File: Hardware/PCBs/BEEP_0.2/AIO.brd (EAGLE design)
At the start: 106.2 x 69.1 mm, 85 parts, among them IC1 ULN2803ASOP18, IC2 ULN2803ASOP18, IC3 74HC238SSOP, IC4 74HC238SSOP, IC5 TS34119SMD, U2 TB6612FNG, U3 ATXMEGA64D3-AU, X1 MICROMATCH-4, X10 MICROMATCH-10, X3 MICROMATCH-8, X4 MICROMATCH-8, X5 MICROMATCH-8, X8 MICROMATCH-8, X9 MICROMATCH-4

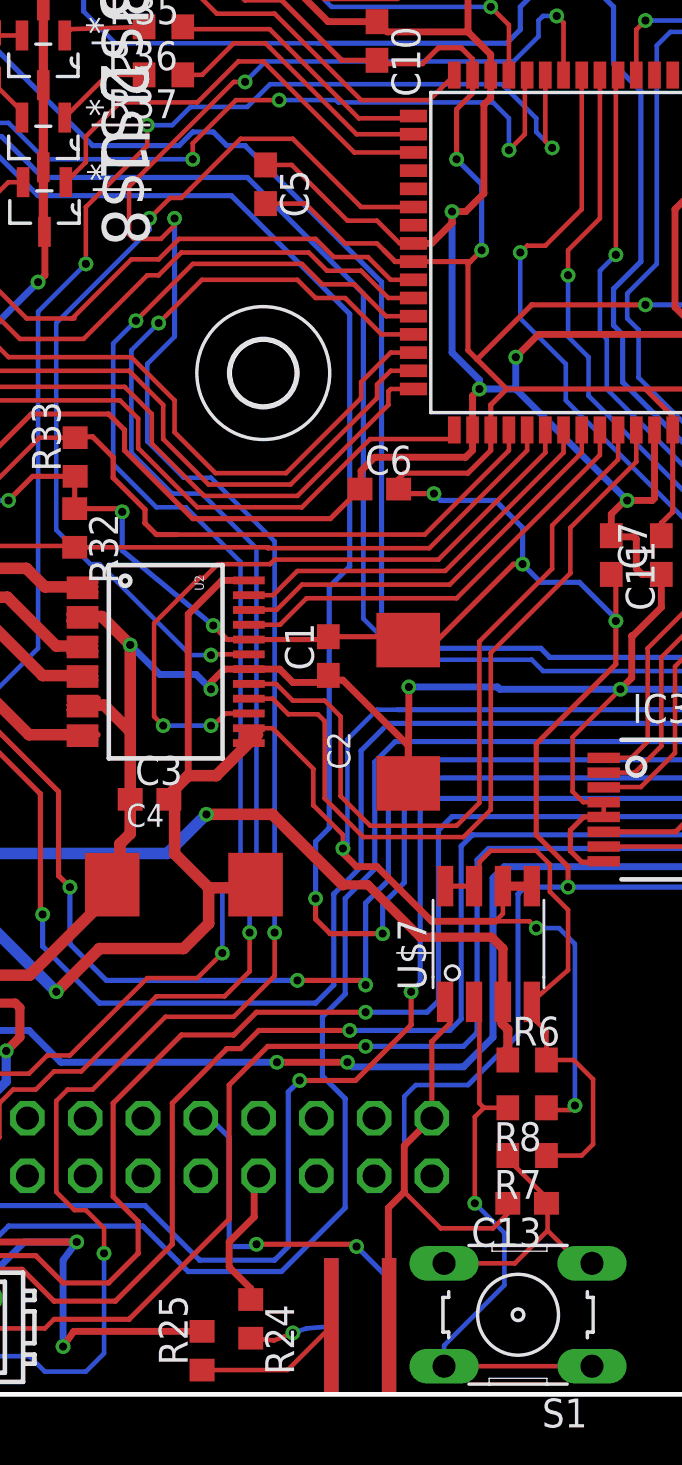
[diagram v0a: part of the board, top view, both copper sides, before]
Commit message: add poweroff line to atxmega
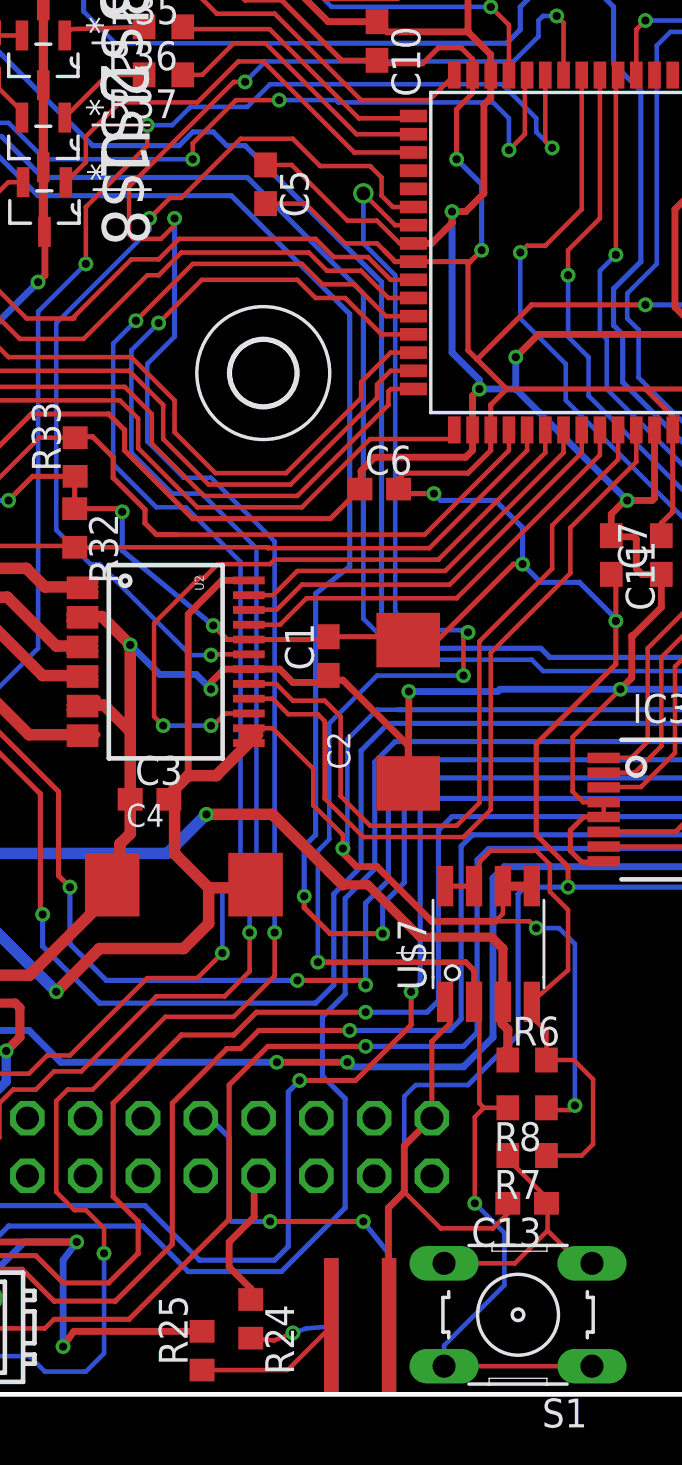
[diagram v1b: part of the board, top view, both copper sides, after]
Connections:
- removed net N$18: R8.2, S1.1, S1.2, U$7.2
- new net POWER_OFF: R8.2, S1.1, S1.2, U$7.2, U3.23
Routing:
- net POWER_OFF: track 0.00 -> 78.8 mm, vias 0 -> 5
- net N$18: track 25.7 -> 0.00 mm, vias 1 -> 0
- net +3V3: track 371.9 -> 368.6 mm
- net IR_LED_K6_OUT: track 114.9 -> 115.4 mm
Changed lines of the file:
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@@
 <wire x1="67.515" y1="36.3" x2="70.1" y2="36.3" width="0.3048" layer="1"/>
 <via x="51.9" y="36.7" extent="1-16" drill="0.3556" shape="octagon"/>
-<wire x1="42.2" y1="36.8" x2="38.3" y2="36.8" width="0.3048" layer="16"/>
-<via x="38.3" y="36.8" extent="1-16" drill="0.3556" shape="octagon"/>
-<wire x1="38.3" y1="36.8" x2="38.3" y2="35.79" width="0.3048" layer="1"/>
+<wire x1="42.2" y1="36.6" x2="38.3" y2="36.6" width="0.3048" layer="16"/>
+<via x="38.3" y="36.6" extent="1-16" drill="0.3556" shape="octagon"/>
+<wire x1="38.3" y1="36.6" x2="38.3" y2="35.79" width="0.3048" layer="1"/>
 <wire x1="38.3" y1="35.79" x2="38.27" y2="32.56" width="0.3048" layer="1"/>
-<wire x1="42.2" y1="36.8" x2="42.3" y2="36.7" width="0.3048" layer="16"/>
+<wire x1="42.2" y1="36.6" x2="42.3" y2="36.7" width="0.3048" layer="16"/>
 <wire x1="60.315" y1="22.5" x2="61.6" y2="22.5" width="0.3048" layer="1"/>
 <wire x1="61.6" y1="22.5" x2="62.1" y2="23" width="0.3048" layer="1"/>
@@
 <wire x1="23.61" y1="44.64" x2="23.61" y2="46.04" width="0.2286" layer="1"/>
 <wire x1="23.61" y1="46.04" x2="23.63" y2="46.06" width="0.2286" layer="1"/>
-<wire x1="37.43" y1="8.69" x2="37.43" y2="10.77" width="0.2286" layer="16"/>
-<wire x1="37.43" y1="10.77" x2="36" y2="12.2" width="0.2286" layer="16"/>
+<wire x1="37.43" y1="8.69" x2="37.43" y2="11.87" width="0.2286" layer="16"/>
+<wire x1="37.43" y1="11.87" x2="36.3" y2="13.3" width="0.2286" layer="16"/>
 <wire x1="29.152" y1="17.844" x2="29.556" y2="17.844" width="0.2286" layer="16"/>
 <wire x1="29.556" y1="17.844" x2="30.4" y2="17" width="0.2286" layer="16"/>
-<wire x1="30.4" y1="17" x2="30.4" y2="12.2" width="0.2286" layer="16"/>
-<wire x1="30.4" y1="12.2" x2="31.5" y2="12.2" width="0.2286" layer="16"/>
-<wire x1="31.5" y1="12.2" x2="31.6" y2="12.3" width="0.2286" layer="16"/>
-<via x="31.6" y="12.3" extent="1-16" drill="0.3556" shape="octagon"/>
-<wire x1="31.6" y1="12.3" x2="35.9" y2="12.3" width="0.2286" layer="1"/>
-<wire x1="35.9" y1="12.3" x2="36" y2="12.2" width="0.2286" layer="1"/>
-<via x="36" y="12.2" extent="1-16" drill="0.3556" shape="octagon"/>
+<via x="32.2" y="13.3" extent="1-16" drill="0.3556" shape="octagon"/>
+<wire x1="32.2" y1="13.3" x2="36.3" y2="13.3" width="0.2286" layer="1"/>
+<via x="36.3" y="13.3" extent="1-16" drill="0.3556" shape="octagon"/>
 <wire x1="12.7" y1="49.53" x2="12.7" y2="52.07" width="0.2286" layer="1"/>
 <wire x1="63.4" y1="13" x2="64.5" y2="11.9" width="0.2286" layer="16"/>
@@
 <wire x1="43.9" y1="34.3" x2="43.9" y2="30.3" width="0.2286" layer="1"/>
 <via x="45.3" y="28" extent="1-16" drill="0.3556" shape="octagon"/>
-<wire x1="37.43" y1="8.69" x2="37.43" y2="13.93" width="0.2032" layer="16"/>
+<wire x1="37.43" y1="11.87" x2="37.43" y2="13.93" width="0.2032" layer="16"/>
 <wire x1="37.43" y1="13.93" x2="38.1" y2="14.6" width="0.2032" layer="16"/>
 <wire x1="38.1" y1="14.6" x2="38.1" y2="18.8" width="0.2032" layer="16"/>
@@
 <wire x1="38.1" y1="46.2" x2="40.9" y2="46.2" width="0.2286" layer="1"/>
 <wire x1="40.9" y1="46.2" x2="41.9" y2="47.2" width="0.2286" layer="1"/>
+<wire x1="32.2" y1="13.3" x2="30.5" y2="13.3" width="0.2286" layer="16"/>
+<wire x1="30.5" y1="13.3" x2="30.4" y2="13.4" width="0.2286" layer="16"/>
+<wire x1="30.4" y1="13.4" x2="30.4" y2="17" width="0.2286" layer="16"/>
 <wire x1="8.832" y1="17.844" x2="29.152" y2="17.844" width="0" layer="19" extent="1-1"/>
 </signal>
@@
 <wire x1="24.3" y1="42.2" x2="22.8" y2="43.7" width="0.2032" layer="16"/>
 <wire x1="22.8" y1="43.7" x2="22.8" y2="52.8" width="0.2032" layer="16"/>
-<wire x1="38.5" y1="57.9" x2="36.2" y2="57.9" width="0.2032" layer="1"/>
-<wire x1="36.2" y1="57.9" x2="33.2" y2="60.9" width="0.2032" layer="1"/>
 <wire x1="33.2" y1="60.9" x2="30.9" y2="60.9" width="0.2032" layer="1"/>
-<wire x1="30.9" y1="60.9" x2="28.7" y2="58.7" width="0.2032" layer="1"/>
+<wire x1="30.9" y1="60.9" x2="28.3" y2="58.3" width="0.2032" layer="1"/>
 <wire x1="22.8" y1="52.8" x2="26.9" y2="56.9" width="0.2032" layer="16"/>
 <wire x1="26.9" y1="56.9" x2="26.9" y2="57.4" width="0.2032" layer="16"/>
 <wire x1="26.9" y1="57.4" x2="27.8" y2="58.3" width="0.2032" layer="1"/>
 <wire x1="27.8" y1="58.3" x2="28.3" y2="58.3" width="0.2032" layer="1"/>
-<wire x1="28.3" y1="58.3" x2="28.7" y2="58.7" width="0.2032" layer="1"/>
+<wire x1="38.5" y1="57.9" x2="37.6" y2="57.9" width="0.2032" layer="1"/>
+<wire x1="37.6" y1="57.9" x2="37.1" y2="58.4" width="0.2032" layer="1"/>
+<wire x1="37.1" y1="58.4" x2="37.1" y2="59.2" width="0.2032" layer="1"/>
+<wire x1="37.1" y1="59.2" x2="36.6" y2="59.7" width="0.2032" layer="1"/>
+<wire x1="36.6" y1="59.7" x2="34.4" y2="59.7" width="0.2032" layer="1"/>
+<wire x1="34.4" y1="59.7" x2="33.2" y2="60.9" width="0.2032" layer="1"/>
 </signal>
 <signal name="MOTOR_A_OUT1">
@@
 </signal>
 <signal name="IR_LED_K6_OUT">
-<via x="34.2" y="27.5" extent="1-16" drill="0.3556" shape="octagon"/>
+<via x="33.7" y="27.6" extent="1-16" drill="0.3556" shape="octagon"/>
 <contactref element="IC2" pad="11"/>
 <via x="13.2" y="62.2" extent="1-16" drill="0.3556" shape="octagon"/>
@@
 <wire x1="38.1" y1="28.2" x2="38.1" y2="32.5" width="0.2286" layer="16"/>
 <wire x1="37.148659375" y1="25.9557875" x2="34.8442125" y2="25.9557875" width="0.2286" layer="1"/>
-<wire x1="34.8442125" y1="25.9557875" x2="34.2" y2="26.6" width="0.2286" layer="1"/>
-<wire x1="34.2" y1="26.6" x2="34.2" y2="27.5" width="0.2286" layer="1"/>
-<wire x1="34.2" y1="27.5" x2="34.2" y2="30" width="0.2286" layer="16"/>
-<wire x1="34.2" y1="30" x2="34.8" y2="30.6" width="0.2286" layer="16"/>
-<wire x1="34.8" y1="30.6" x2="34.8" y2="41.2" width="0.2286" layer="16"/>
+<wire x1="34.8442125" y1="25.9557875" x2="33.7" y2="27.1" width="0.2286" layer="1"/>
+<wire x1="33.7" y1="27.1" x2="33.7" y2="27.6" width="0.2286" layer="1"/>
+<wire x1="33.7" y1="27.6" x2="33.7" y2="29.8" width="0.2286" layer="16"/>
+<wire x1="33.7" y1="29.8" x2="34.2" y2="30.3" width="0.2286" layer="16"/>
+<wire x1="34.2" y1="30.3" x2="34.2" y2="40.9" width="0.2286" layer="16"/>
 <wire x1="35.7" y1="53.2" x2="35.7" y2="42.1" width="0.2286" layer="16"/>
-<wire x1="35.7" y1="42.1" x2="34.8" y2="41.2" width="0.2286" layer="16"/>
+<wire x1="35.7" y1="42.1" x2="34.2" y2="40.9" width="0.2286" layer="16"/>
 <wire x1="20.2" y1="60.2" x2="22" y2="58.4" width="0.2286" layer="16"/>
 <wire x1="22" y1="58.4" x2="30.5" y2="58.4" width="0.2286" layer="16"/>
@@
 <wire x1="43" y1="15.85" x2="42.65" y2="16.2" width="0.2032" layer="1"/>
 </signal>
-<signal name="N$18">
+<signal name="POWER_OFF">
 <contactref element="R8" pad="2"/>
 <contactref element="U$7" pad="2"/>
@@
 <wire x1="41.6" y1="18.3" x2="42.65" y2="18.3" width="0.2032" layer="1"/>
 <wire x1="41.4" y1="18.5" x2="41.6" y2="18.3" width="0.2032" layer="1"/>
+<contactref element="U3" pad="23"/>
+<wire x1="41.165" y1="22.9568" x2="41.165" y2="24.335" width="0.254" layer="1"/>
+<wire x1="41.165" y1="24.335" x2="40.8" y2="24.7" width="0.254" layer="1"/>
+<wire x1="40.8" y1="24.7" x2="34.3" y2="24.7" width="0.254" layer="1"/>
+<wire x1="38.5" y1="57.1" x2="37.7" y2="57.1" width="0.2032" layer="1"/>
+<wire x1="37.7" y1="57.1" x2="36.3" y2="58.5" width="0.2032" layer="1"/>
+<via x="36.3" y="58.5" extent="1-16" drill="0.6" shape="square"/>
+<wire x1="36.3" y1="58.5" x2="36.3" y2="56.3" width="0.2032" layer="16"/>
+<wire x1="36.3" y1="56.3" x2="37.7" y2="54.9" width="0.2032" layer="16"/>
+<wire x1="37.7" y1="54.9" x2="37.7" y2="40.1" width="0.2032" layer="16"/>
+<wire x1="37.7" y1="40.1" x2="38.5" y2="39.3" width="0.2032" layer="16"/>
+<wire x1="38.5" y1="39.3" x2="40.8" y2="39.3" width="0.2032" layer="16"/>
+<wire x1="40.8" y1="39.3" x2="40.9" y2="39.2" width="0.2032" layer="16"/>
+<via x="40.9" y="39.2" extent="1-16" drill="0.3556" shape="octagon"/>
+<via x="40.7" y="37.3" extent="1-16" drill="0.3556" shape="octagon"/>
+<wire x1="40.7" y1="37.3" x2="36.9" y2="37.3" width="0.2032" layer="16"/>
+<wire x1="36.9" y1="37.3" x2="34.8" y2="35.2" width="0.2032" layer="16"/>
+<wire x1="34.8" y1="35.2" x2="34.8" y2="30.1" width="0.2032" layer="16"/>
+<wire x1="34.8" y1="30.1" x2="34.3" y2="29.6" width="0.2032" layer="16"/>
+<wire x1="34.3" y1="29.6" x2="34.3" y2="24.7" width="0.2032" layer="16"/>
+<via x="34.3" y="24.7" extent="1-16" drill="0.3556" shape="octagon"/>
+<wire x1="40.7" y1="37.3" x2="40.7" y2="39" width="0.2032" layer="1"/>
+<wire x1="40.7" y1="39" x2="40.9" y2="39.2" width="0.2032" layer="1"/>
 </signal>
 <signal name="N$22">

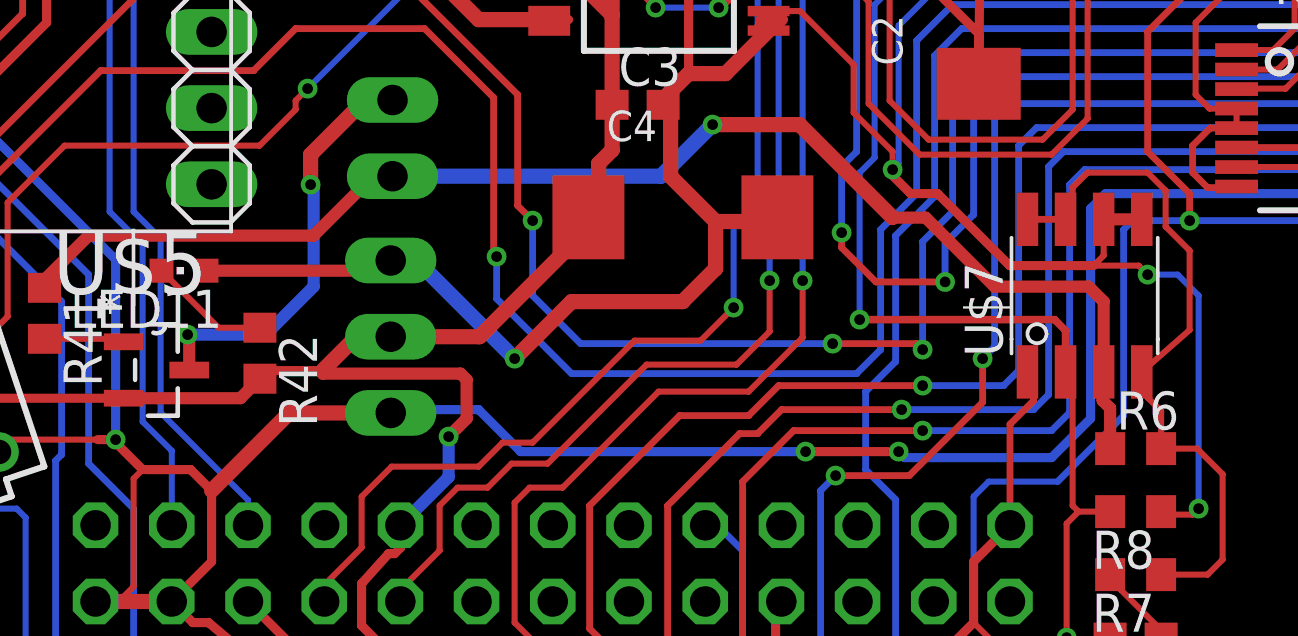
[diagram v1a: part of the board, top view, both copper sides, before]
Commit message: enhance routing fix rgb and ir distance board (connector was on the wrong side)
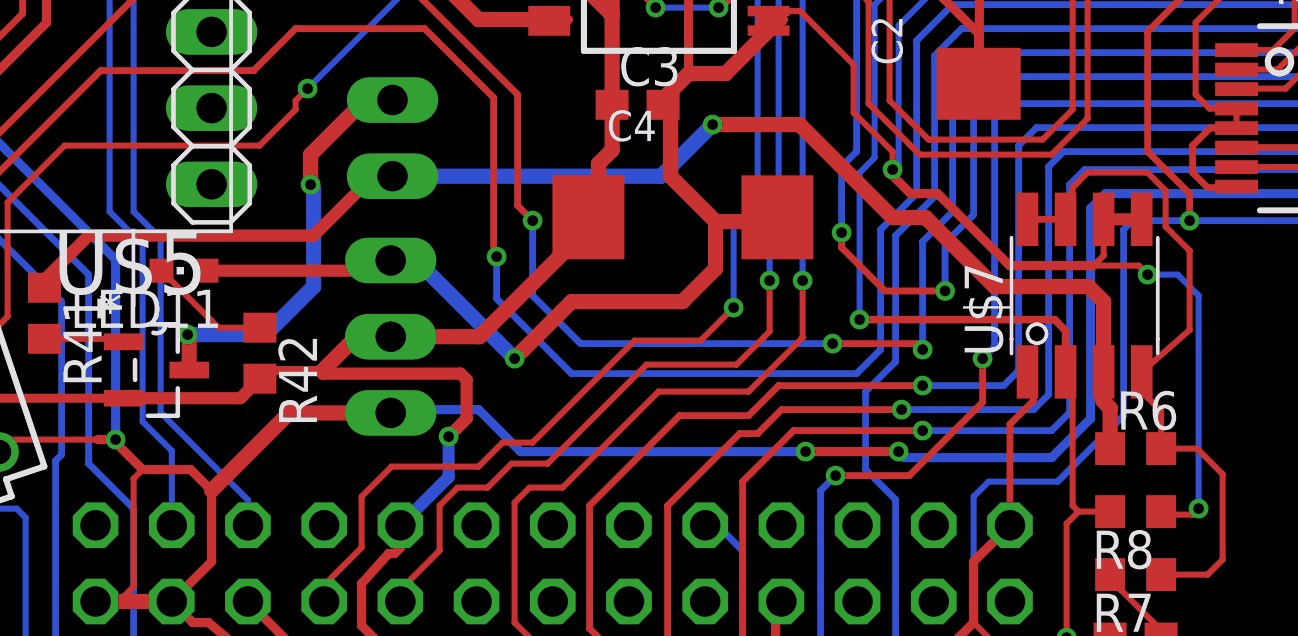
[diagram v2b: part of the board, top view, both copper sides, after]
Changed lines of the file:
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@@
 <wire x1="18.71" y1="32" x2="18.73" y2="32.02" width="0.508" layer="1"/>
 <contactref element="U$5" pad="D"/>
-<wire x1="11.9" y1="24.2" x2="14.5" y2="24.2" width="0.4064" layer="16"/>
-<wire x1="14.5" y1="24.2" x2="16.1" y2="25.8" width="0.4064" layer="16"/>
-<wire x1="16.1" y1="25.8" x2="16.1" y2="29.1" width="0.4064" layer="16"/>
+<wire x1="11.9" y1="24.2" x2="14.5" y2="24.2" width="0.508" layer="16"/>
+<wire x1="14.5" y1="24.2" x2="16.1" y2="25.8" width="0.508" layer="16"/>
+<wire x1="16.1" y1="25.8" x2="16.1" y2="29.1" width="0.508" layer="16"/>
 <wire x1="16.1" y1="29.1" x2="16" y2="29.2" width="0.4064" layer="16"/>
-<wire x1="11.9522" y1="23.02" x2="11.9522" y2="24.1478" width="0.4064" layer="1"/>
+<wire x1="11.9522" y1="23.02" x2="11.9522" y2="24.1478" width="0.508" layer="1"/>
 <wire x1="11.9522" y1="24.1478" x2="11.9" y2="24.2" width="0.4064" layer="1"/>
 </signal>
@@
 <wire x1="51.5" y1="32.8" x2="38.4" y2="32.8" width="0.2286" layer="16"/>
 <wire x1="38.4" y1="32.8" x2="38.1" y2="32.5" width="0.2286" layer="16"/>
-<via x="37.148659375" y="25.9557875" extent="1-16" drill="0.3556" shape="octagon"/>
-<wire x1="37.148659375" y1="25.9557875" x2="37.148659375" y2="27.248659375" width="0.2286" layer="16"/>
+<via x="37.148659375" y="25.6557875" extent="1-16" drill="0.3556" shape="octagon"/>
+<wire x1="37.148659375" y1="25.6557875" x2="37.148659375" y2="27.248659375" width="0.2286" layer="16"/>
 <wire x1="37.148659375" y1="27.248659375" x2="38.1" y2="28.2" width="0.2286" layer="16"/>
 <wire x1="38.1" y1="28.2" x2="38.1" y2="32.5" width="0.2286" layer="16"/>
-<wire x1="37.148659375" y1="25.9557875" x2="34.8442125" y2="25.9557875" width="0.2286" layer="1"/>
-<wire x1="34.8442125" y1="25.9557875" x2="33.7" y2="27.1" width="0.2286" layer="1"/>
+<wire x1="37.148659375" y1="25.6557875" x2="35.1442125" y2="25.6557875" width="0.2286" layer="1"/>
+<wire x1="35.1442125" y1="25.6557875" x2="33.7" y2="27.1" width="0.2286" layer="1"/>
 <wire x1="33.7" y1="27.1" x2="33.7" y2="27.6" width="0.2286" layer="1"/>
 <wire x1="33.7" y1="27.6" x2="33.7" y2="29.8" width="0.2286" layer="16"/>
@@
 <wire x1="18.1" y1="29.5" x2="18.71" y2="29.5" width="0.4064" layer="1"/>
 <wire x1="18.71" y1="29.5" x2="18.73" y2="29.48" width="0.4064" layer="1"/>
-<wire x1="35.4" y1="28.1" x2="36.5" y2="28.1" width="0.4064" layer="1"/>
-<wire x1="36.5" y1="28.1" x2="38.8" y2="25.8" width="0.4064" layer="1"/>
-<wire x1="38.8" y1="25.8" x2="41.935" y2="25.8" width="0.4064" layer="1"/>
-<wire x1="41.935" y1="25.8" x2="42.435" y2="25.3" width="0.4064" layer="1"/>
-<wire x1="42.435" y1="25.3" x2="42.435" y2="22.9568" width="0.4064" layer="1"/>
-<wire x1="42.65" y1="20.4" x2="42.65" y2="21.75" width="0.4064" layer="1"/>
-<wire x1="42.65" y1="21.75" x2="42.4" y2="22" width="0.4064" layer="1"/>
+<wire x1="35.4" y1="28.1" x2="36.5" y2="28.1" width="0.508" layer="1"/>
+<wire x1="36.5" y1="28.1" x2="38.8" y2="25.8" width="0.508" layer="1"/>
+<wire x1="38.8" y1="25.8" x2="41.935" y2="25.8" width="0.508" layer="1"/>
+<wire x1="41.935" y1="25.8" x2="42.435" y2="25.3" width="0.508" layer="1"/>
+<wire x1="42.435" y1="25.3" x2="42.435" y2="22.9568" width="0.508" layer="1"/>
+<wire x1="42.65" y1="20.4" x2="42.65" y2="21.75" width="0.508" layer="1"/>
+<wire x1="42.65" y1="21.75" x2="42.4" y2="22" width="0.508" layer="1"/>
 <wire x1="42.4" y1="22" x2="42.4" y2="22.9218" width="0.4064" layer="1"/>
 <wire x1="42.4" y1="22.9218" x2="42.435" y2="22.9568" width="0.4064" layer="1"/>
